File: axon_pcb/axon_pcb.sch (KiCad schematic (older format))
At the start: 104 parts, among them J1 USB_C_Receptacle, J2 AVR_ISP Header, K1 KEYSW, K10 KEYSW, K11 KEYSW, K12 KEYSW, K13 KEYSW, K14 KEYSW, K15 KEYSW, K16 KEYSW, K17 KEYSW, K18 KEYSW, K19 KEYSW, K2 KEYSW, K20 KEYSW, K21 KEYSW, K22 KEYSW, K23 KEYSW, K24 KEYSW, K25 KEYSW, K26 KEYSW, K27 KEYSW, K28 KEYSW, K29 KEYSW, K3 KEYSW, K30 KEYSW, K31 KEYSW, K32 KEYSW, K33 KEYSW, K34 KEYSW, K35 KEYSW, K36 KEYSW, K37 KEYSW, K38 KEYSW, K39 KEYSW, K4 KEYSW, K40 KEYSW, K41 KEYSW, K42 KEYSW, K43 KEYSW, K44 KEYSW, K5 KEYSW, K6 KEYSW, K7 KEYSW, K8 KEYSW, K9 KEYSW, SW1 RESET, SW2 BOOT, U1 ATmega328P-PU, X1 16MHz

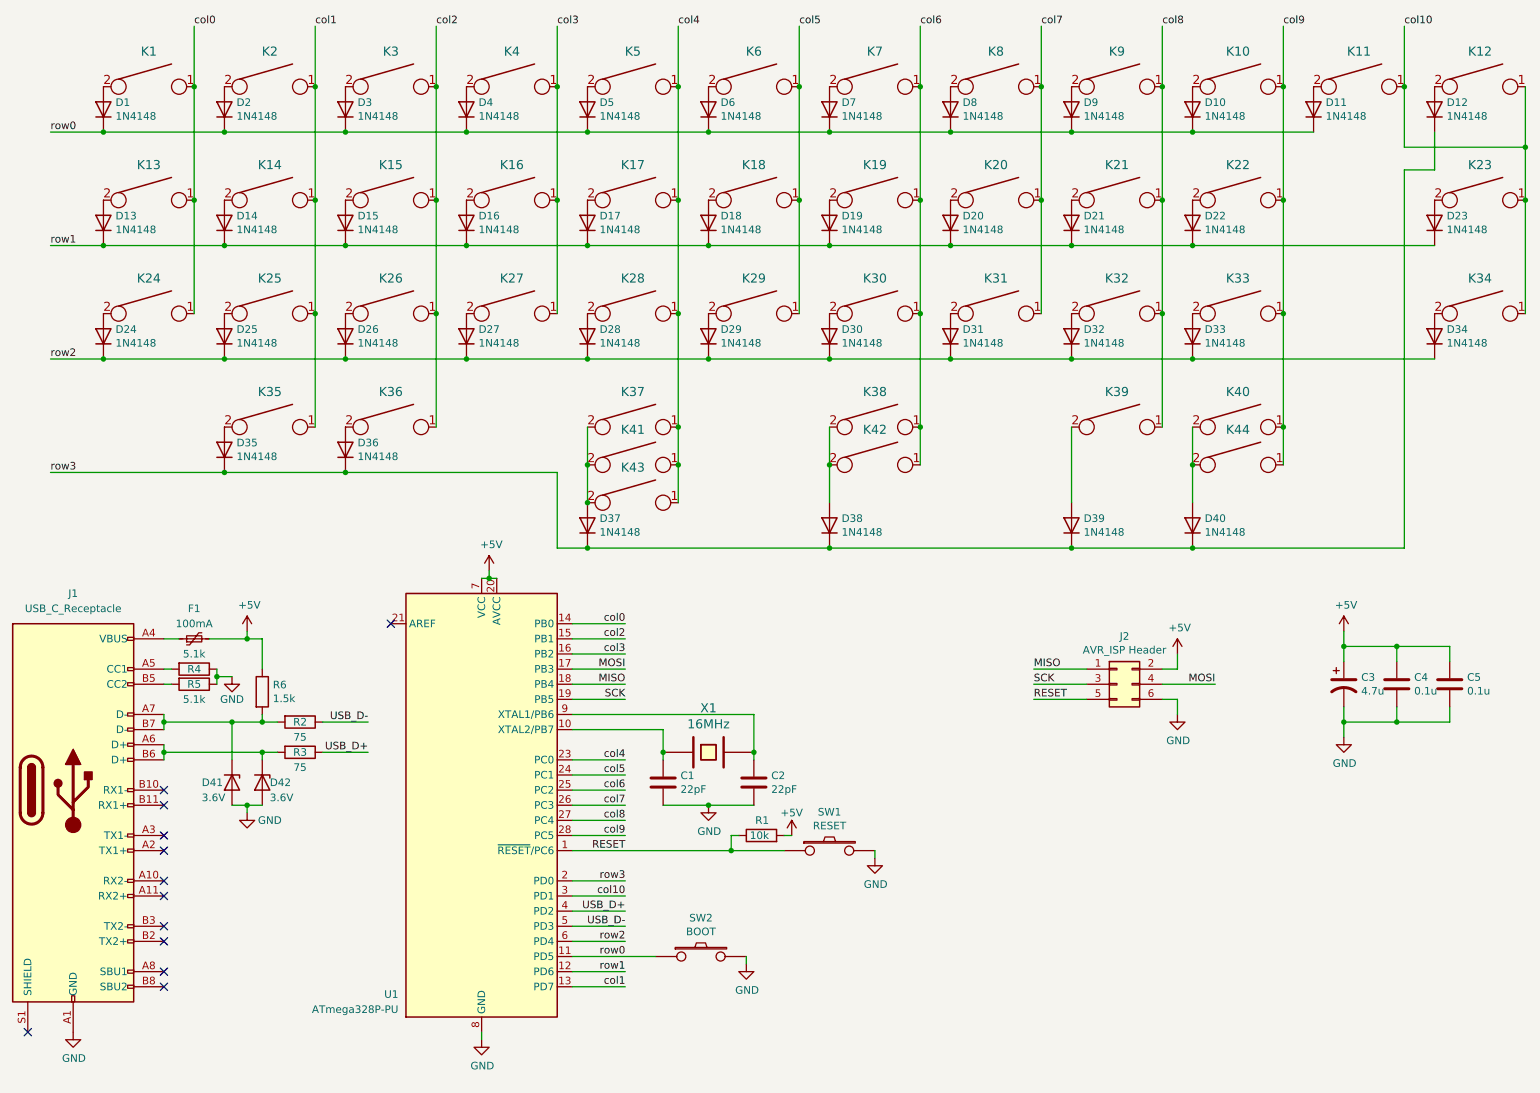
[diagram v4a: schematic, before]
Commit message: adjusted footprints, added 6.25u support
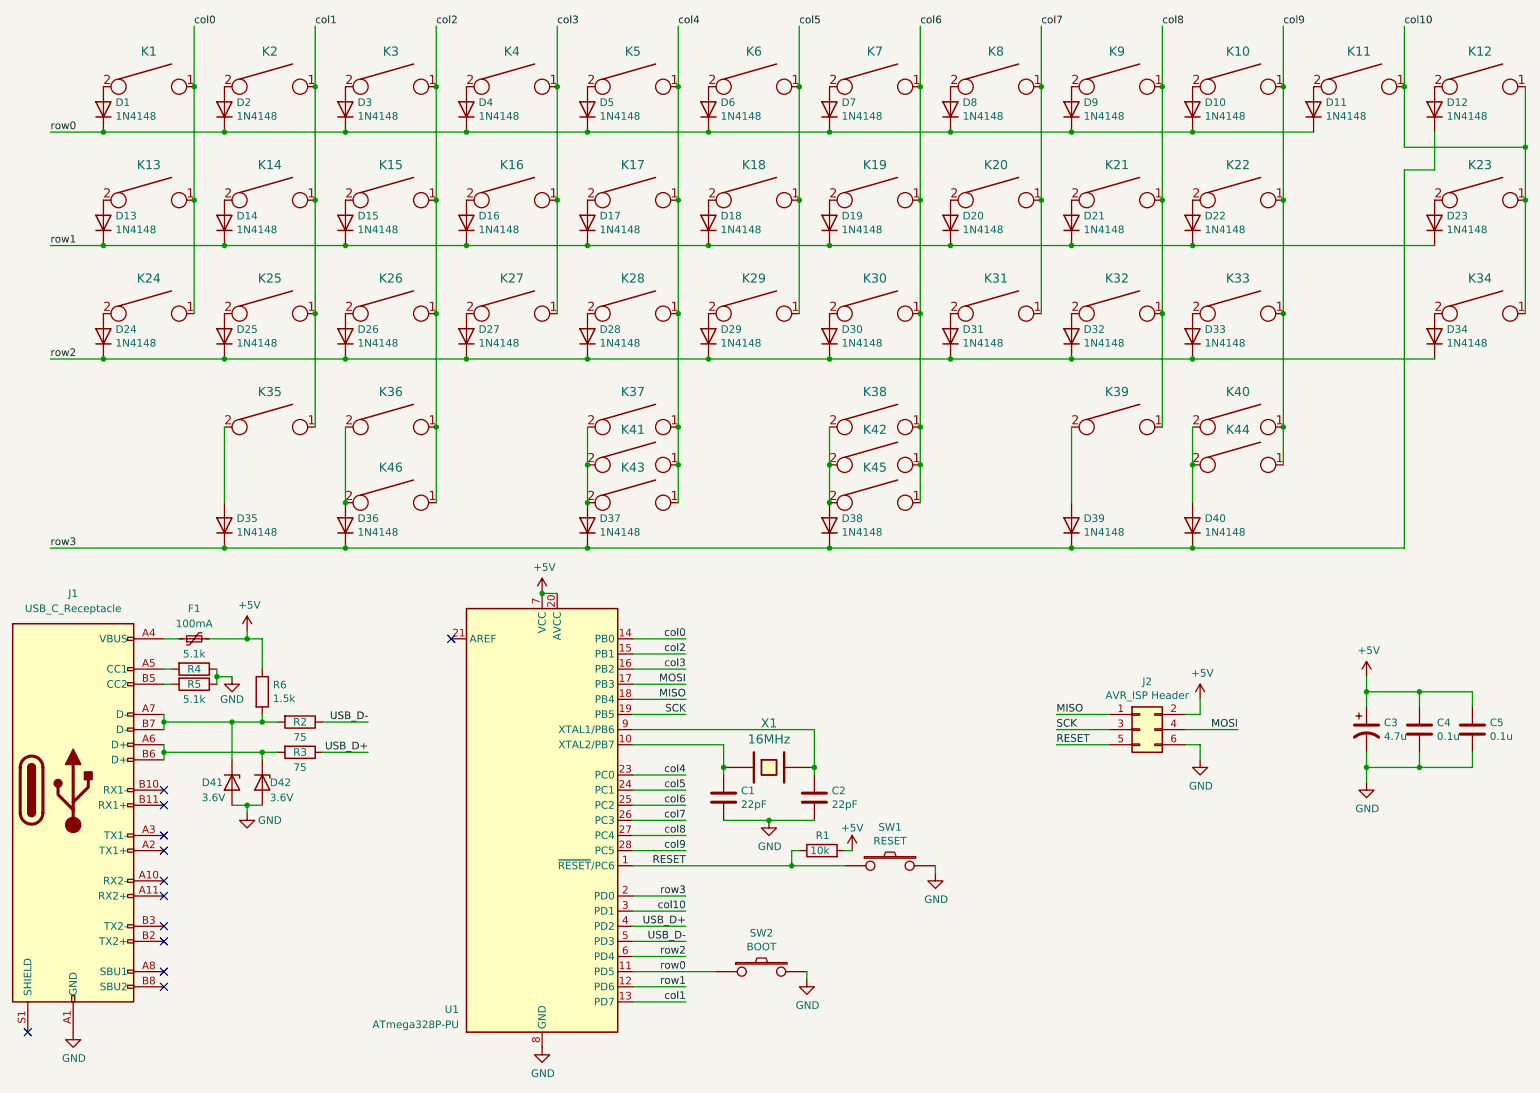
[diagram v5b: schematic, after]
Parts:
- added K45, K46: KEYSW, personal:SW_MX_Minimal_InsideSilkRef, symbol keyboard-parts:KEYSW
- K1, K10, K11, K12, K13, K14, K15, K16, K17, K18, K19, K2, K20, K21, K22, K23, K24, K25, K26, K27, K28, K29, K3, K30, K31, K32, K33, K34, K4, K5, K6, K7, K8, K9: footprint keyswitches-daprice:SW_MX -> personal:SW_MX_InsideSilkRef
- K35, K36, K37, K38, K39, K40, K41, K42, K43, K44: footprint keyswitches-daprice:SW_MX -> personal:SW_MX_Minimal_InsideSilkRef
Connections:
- net col2: now also K46.1
- net col6: now also K45.1
- net at D36.2 (A), K36.2: now also K46.2
- net at D38.2 (A), K38.2, K42.2: now also K45.2
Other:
- moved on the sheet: C1, C2, C3, C4, C5, D35, D36, J2, R1, SW1, SW2, U1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

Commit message: updated usb4085 footprint for easier handsoldering, added spacebar notes to schema
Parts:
- J1: footprint Connector_USB:USB_C_Receptacle_GCT_USB4085 -> personal:USB_C_Receptacle_GCT_USB4085_personalized
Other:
- note added: "2.25u L spacebar"
- note added: "2.25u R spacebar"
- note added: "2.75u L spacebar"
- note added: "2.75u R spacebar"
- note added: "6.25u spacebar"
- note added: "7u spacebar"
- moved on the sheet: K44
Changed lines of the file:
@@
 F 0 "J1" H 1100 7150 50  0000 C CNN
 F 1 "USB_C_Receptacle" H 1100 7050 50  0000 C CNN
-F 2 "Connector_USB:USB_C_Receptacle_GCT_USB4085" H 1250 5850 50  0001 C CNN
+F 2 "personal:USB_C_Receptacle_GCT_USB4085_personalized" H 1250 5850 50  0001 C CNN
 F 3 "https://www.usb.org/sites/default/files/documents/usb_type-c.zip" H 1250 5850 50  0001 C CNN
 	1    1100 5850
@@
 L keyboard-parts:KEYSW K44
 U 1 1 609D318E
-P 8800 3700
-F 0 "K44" H 8800 3933 60  0000 C CNN
-F 1 "KEYSW" H 8800 3600 60  0001 C CNN
-F 2 "personal:SW_MX_Minimal_InsideSilkRef" H 8800 3700 60  0001 C CNN
-F 3 "" H 8800 3700 60  0000 C CNN
-	1    8800 3700
-	1    0    0    -1
-$EndComp
-Wire Wire Line
-	9100 3450 9100 3700
+P 8800 3950
+F 0 "K44" H 8800 4183 60  0000 C CNN
+F 1 "KEYSW" H 8800 3850 60  0001 C CNN
+F 2 "personal:SW_MX_Minimal_InsideSilkRef" H 8800 3950 60  0001 C CNN
+F 3 "" H 8800 3950 60  0000 C CNN
+	1    8800 3950
+	1    0    0    -1
+$EndComp
+Wire Wire Line
+	9100 3450 9100 3950
 Connection ~ 9100 3450
 Wire Wire Line
-	8500 3450 8500 3700
+	8500 3450 8500 3950
 Wire Wire Line
 	9900 1750 9900 4250
@@
 Wire Wire Line
 	7700 3450 7700 3950
-Wire Wire Line
-	8500 3700 8500 3950
-Connection ~ 8500 3700
+Connection ~ 8500 3950
 $Comp
 L keyboard-parts:KEYSW K45
@@
 	3500 3450 3500 3950
 Connection ~ 3500 3450
+Text Notes 6750 3950 0    50   ~ 0
+6.25u spacebar
+Text Notes 6750 3700 0    50   ~ 0
+2.75u R spacebar
+Text Notes 6750 3450 0    50   ~ 0
+2.25u R spacebar
+Text Notes 5150 3450 0    50   ~ 0
+2.75u L spacebar
+Text Notes 5150 3700 0    50   ~ 0
+2.25u L spacebar
+Text Notes 5150 3950 0    50   ~ 0
+7u spacebar
 $EndSCHEMATC

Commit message: minor layout tweaks
- Increased compactness of components below USB connector
- Reduced length mismatch of USB data lines
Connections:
- net D-: now reaches D41.1 (K), J1.A7 (D-), J1.B7 (D-), R2.2, R6.2
- net D+: now reaches D42.1 (K), J1.A6 (D+), J1.B6 (D+), R3.2
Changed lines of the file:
@@
 Text Notes 5150 3950 0    50   ~ 0
 7u spacebar
+Text Label 1800 5400 0    50   ~ 0
+D-
+Text Label 1800 5600 0    50   ~ 0
+D+
 $EndSCHEMATC

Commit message: minor routing changes
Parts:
- F1: value 100mA -> 250mA
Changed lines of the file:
@@
 P 1900 4850
 F 0 "F1" V 2100 4850 50  0000 C CNN
-F 1 "100mA" V 2000 4850 50  0000 C CNN
+F 1 "250mA" V 2000 4850 50  0000 C CNN
 F 2 "Capacitor_THT:C_Disc_D5.0mm_W2.5mm_P5.00mm" H 1950 4650 50  0001 L CNN
 F 3 "~" H 1900 4850 50  0001 C CNN
